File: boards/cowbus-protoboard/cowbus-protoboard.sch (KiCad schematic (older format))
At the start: 3 parts, among them P1 CPU_TO_PERIPH, P2 PERIPH_TO_MCU, P7 CONN_01X01

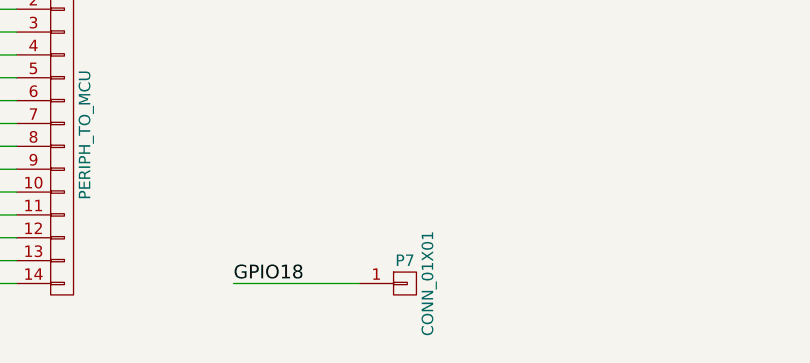
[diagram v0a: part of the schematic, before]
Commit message: added schematics rev, annotation fixed, OSHW logo
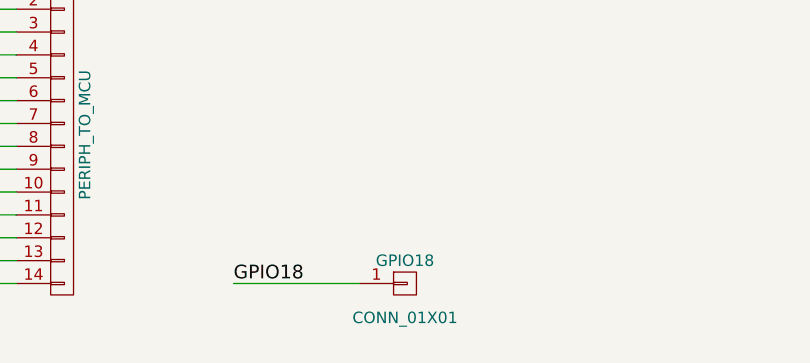
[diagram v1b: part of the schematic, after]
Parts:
- renumbered P7 to GPIO18
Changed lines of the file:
@@
 Sheet 1 6
 Title "cowbus protoboard"
-Date "2015-07-15"
-Rev "0.9"
+Date "2015-08-02"
+Rev "1"
 Comp ""
 Comment1 ""
@@
 3V3
 $Comp
-L CONN_01X01 P7
+L CONN_01X01 GPIO18
 U 1 1 55BD6FBA
 P 5300 7150
-F 0 "P7" H 5300 7250 50  0000 C CNN
-F 1 "CONN_01X01" V 5400 7150 50  0000 C CNN
+F 0 "GPIO18" H 5300 7250 50  0000 C CNN
+F 1 "CONN_01X01" H 5300 7000 50  0000 C CNN
 F 2 "Pin_Headers:Pin_Header_Straight_1x01" H 5300 7150 60  0001 C CNN
 F 3 "" H 5300 7150 60  0000 C CNN
